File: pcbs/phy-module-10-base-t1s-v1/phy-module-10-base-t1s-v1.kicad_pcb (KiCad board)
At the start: 6 copper layers, 25 x 25 mm, 102 parts, among them J201 JST-GH-2-Vertical, J202 JST-GH-2-Vertical, J501 PHY Interface V2 Plug, Q301 DMN21D2UFB-7B, Q601 DMN21D2UFB-7B, U301 LMQ66420MC3RXBRQ1, U302 TPS16410DRCR, U303 TPS7B8133QDRVRQ1, U304 TPS7B8133QDRVRQ1, U305 TPS2116DRL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

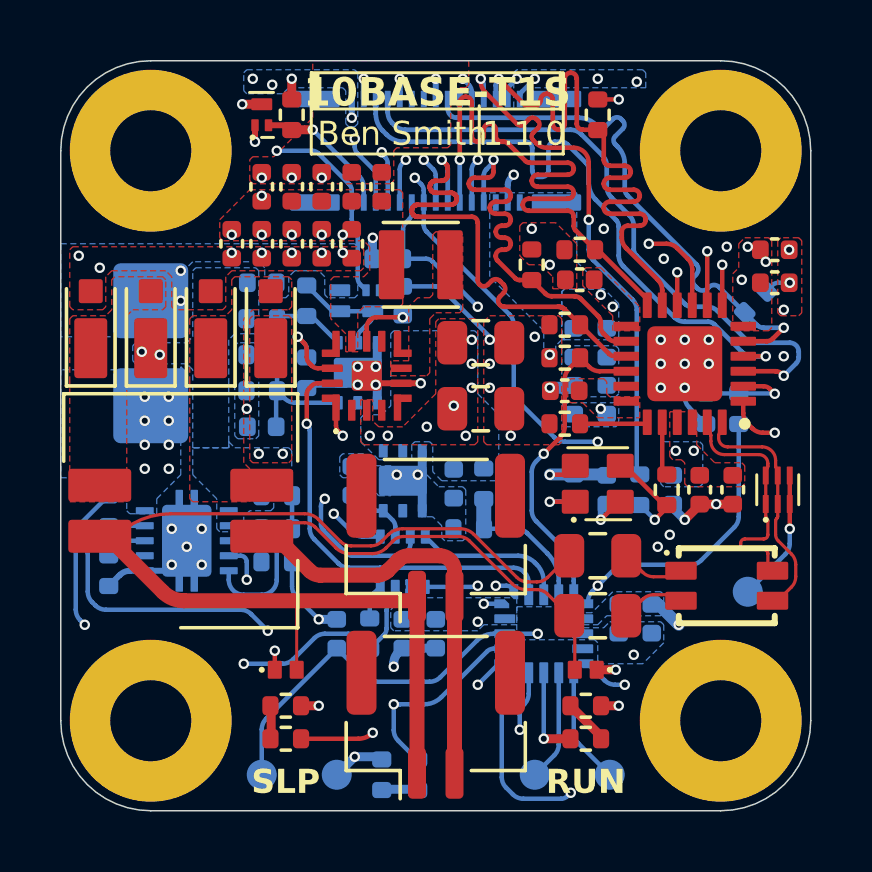
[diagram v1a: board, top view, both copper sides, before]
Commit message: [10base-t1s-v1] Added config without PoDL
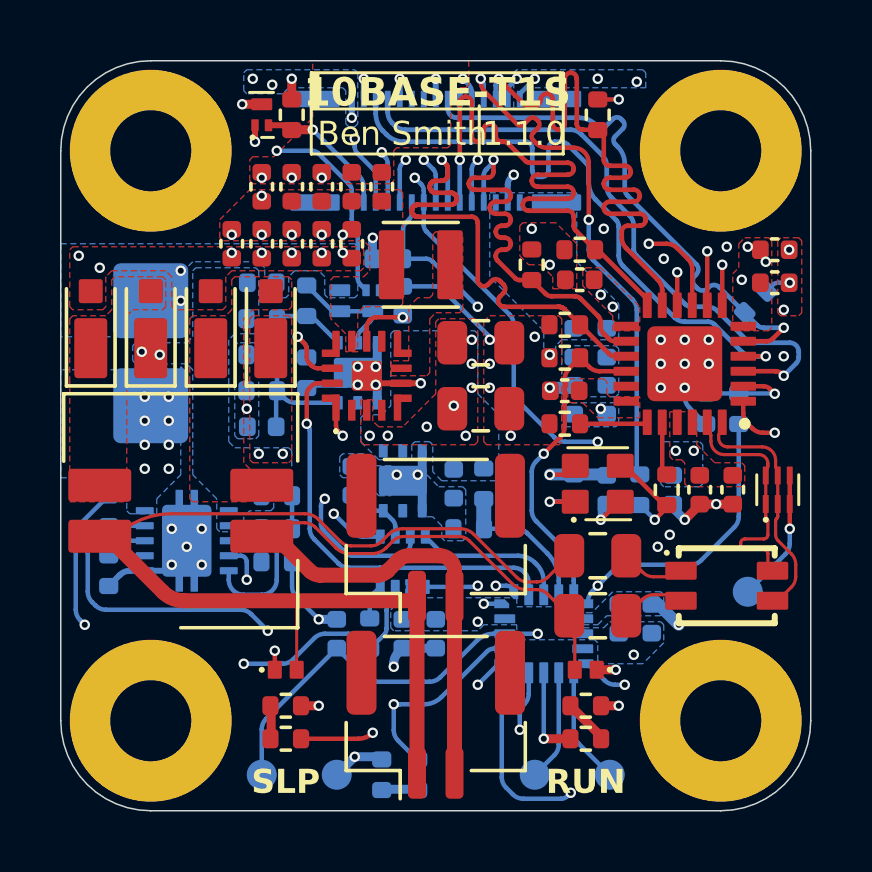
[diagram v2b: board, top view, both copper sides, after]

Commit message: [10base-t1s-v1] Updated LED footprints
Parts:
- D601, D602, D603: footprint project_footprints:R_0402 -> project_footprints:LED_0402
